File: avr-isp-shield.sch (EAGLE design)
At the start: 14 parts, among them IC1 ATTINY24/44/84-PU, U2 TINY45-20-DIP, U3 ATMEGA328P_PDIP, U4 ARDUINOR3-DIMENSION

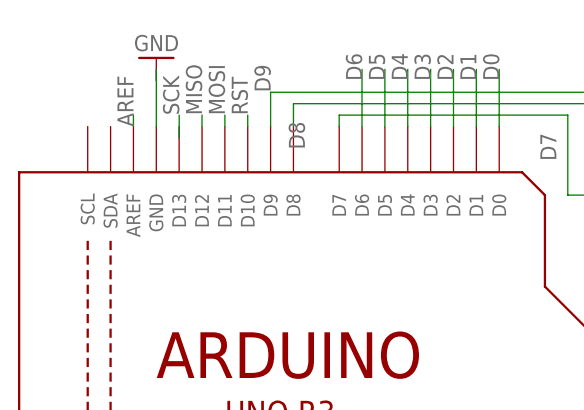
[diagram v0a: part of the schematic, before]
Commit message: routing SCK correctly
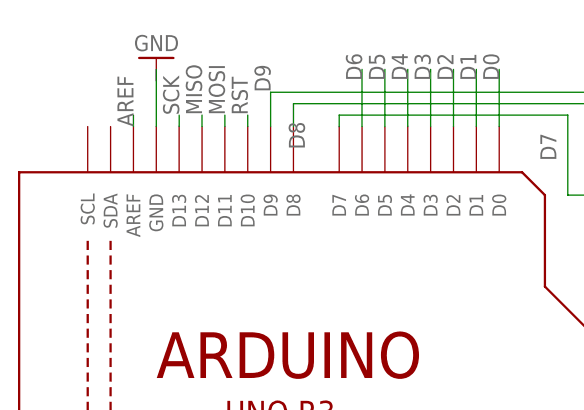
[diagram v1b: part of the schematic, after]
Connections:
- net SCK: now also U4.D13
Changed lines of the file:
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@@
-</segment>
-<segment>
-<wire x1="20.32" y1="115.57" x2="20.32" y2="118.11" width="0.1524" layer="91"/>
-<label x="20.32" y="118.11" size="1.778" layer="95" rot="R90"/>
 </segment>
 <segment>
@@
 <label x="67.31" y="52.07" size="1.778" layer="95"/>
 </segment>
+<segment>
+<pinref part="U4" gate="G$1" pin="D13"/>
+<wire x1="20.32" y1="116.84" x2="20.32" y2="118.11" width="0.1524" layer="91"/>
+<label x="20.32" y="118.11" size="1.778" layer="95" rot="R90"/>
+</segment>
 </net>

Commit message: v1
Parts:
- R1, R2, R3: value 500Ohm -> 500
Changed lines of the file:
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@@
 <part name="IC1" library="attiny24_44_84" deviceset="ATTINY24/44/84" device="-PU"/>
 <part name="C1" library="SparkFun-Passives" deviceset="CAP_POL" device="PTH2" value="10uF"/>
-<part name="R1" library="SparkFun-Passives" deviceset="RESISTOR" device="AXIAL-0.3" value="500Ohm"/>
-<part name="R2" library="SparkFun-Passives" deviceset="RESISTOR" device="AXIAL-0.3" value="500Ohm"/>
-<part name="R3" library="SparkFun-Passives" deviceset="RESISTOR" device="AXIAL-0.3" value="500Ohm"/>
+<part name="R1" library="SparkFun-Passives" deviceset="RESISTOR" device="AXIAL-0.3" value="500"/>
+<part name="R2" library="SparkFun-Passives" deviceset="RESISTOR" device="AXIAL-0.3" value="500"/>
+<part name="R3" library="SparkFun-Passives" deviceset="RESISTOR" device="AXIAL-0.3" value="500"/>
 <part name="LED1" library="SparkFun-LED" deviceset="LED" device="3MM"/>
 <part name="LED2" library="SparkFun-LED" deviceset="LED" device="3MM"/>
